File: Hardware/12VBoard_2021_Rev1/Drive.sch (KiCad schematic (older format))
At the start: 33 parts

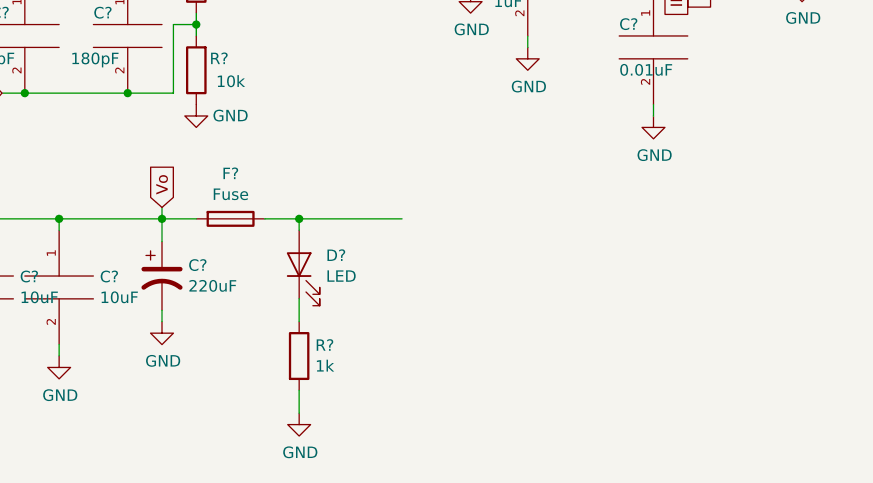
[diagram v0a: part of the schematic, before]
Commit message: current sense
started current sense circuit on hig current. added fuse and LED signal. started tiva wiring.
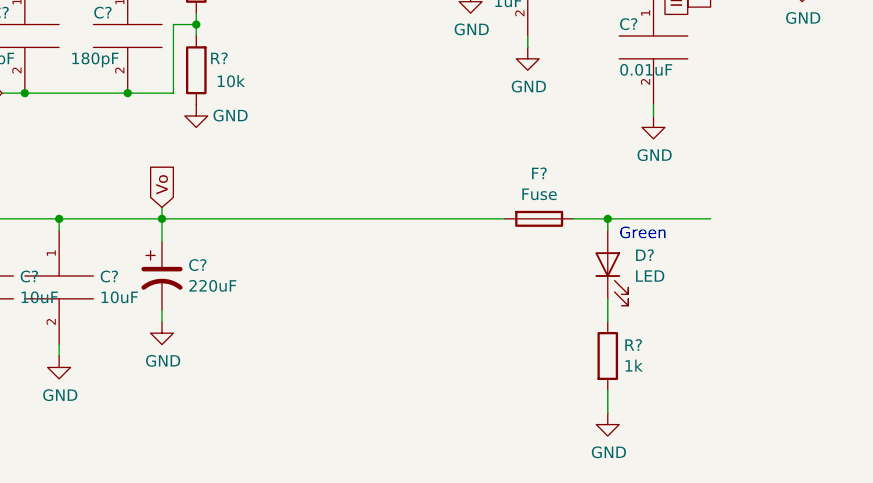
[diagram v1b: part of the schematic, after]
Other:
- note added: "Green"
- moved on the sheet: D?, F?, R?
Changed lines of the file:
@@
 L Device:Fuse F?
 U 1 1 5F97A572
-P 3150 3350
-F 0 "F?" V 2953 3350 50  0000 C CNN
-F 1 "Fuse" V 3044 3350 50  0000 C CNN
-F 2 "" V 3080 3350 50  0001 C CNN
-F 3 "~" H 3150 3350 50  0001 C CNN
-	1    3150 3350
+P 4500 3350
+F 0 "F?" V 4303 3350 50  0000 C CNN
+F 1 "Fuse" V 4394 3350 50  0000 C CNN
+F 2 "" V 4430 3350 50  0001 C CNN
+F 3 "~" H 4500 3350 50  0001 C CNN
+	1    4500 3350
 	0    1    1    0
 $EndComp
 Wire Wire Line
-	3000 3350 2850 3350
-Wire Wire Line
-	3300 3350 3450 3350
+	4650 3350 4800 3350
 $Comp
 L Device:R R?
 U 1 1 5F985FB9
-P 3450 3950
-F 0 "R?" H 3520 3996 50  0000 L CNN
-F 1 "1k" H 3520 3905 50  0000 L CNN
-F 2 "" V 3380 3950 50  0001 C CNN
-F 3 "~" H 3450 3950 50  0001 C CNN
-	1    3450 3950
+P 4800 3950
+F 0 "R?" H 4870 3996 50  0000 L CNN
+F 1 "1k" H 4870 3905 50  0000 L CNN
+F 2 "" V 4730 3950 50  0001 C CNN
+F 3 "~" H 4800 3950 50  0001 C CNN
+	1    4800 3950
 	1    0    0    -1
 $EndComp
@@
 L power:GND #PWR?
 U 1 1 5F98656C
-P 3450 4200
-F 0 "#PWR?" H 3450 3950 50  0001 C CNN
-F 1 "GND" H 3455 4027 50  0000 C CNN
-F 2 "" H 3450 4200 50  0001 C CNN
-F 3 "" H 3450 4200 50  0001 C CNN
-	1    3450 4200
+P 4800 4200
+F 0 "#PWR?" H 4800 3950 50  0001 C CNN
+F 1 "GND" H 4805 4027 50  0000 C CNN
+F 2 "" H 4800 4200 50  0001 C CNN
+F 3 "" H 4800 4200 50  0001 C CNN
+	1    4800 4200
 	1    0    0    -1
 $EndComp
@@
 L Device:LED D?
 U 1 1 5F986D88
-P 3450 3550
-F 0 "D?" V 3489 3433 50  0000 R CNN
-F 1 "LED" V 3398 3433 50  0000 R CNN
-F 2 "" H 3450 3550 50  0001 C CNN
-F 3 "~" H 3450 3550 50  0001 C CNN
-	1    3450 3550
+P 4800 3550
+F 0 "D?" V 4839 3433 50  0000 R CNN
+F 1 "LED" V 4748 3433 50  0000 R CNN
+F 2 "" H 4800 3550 50  0001 C CNN
+F 3 "~" H 4800 3550 50  0001 C CNN
+	1    4800 3550
 	0    -1   -1   0
 $EndComp
@@
 	2850 3800 2850 3750
 Wire Wire Line
-	3450 4200 3450 4100
+	4800 4200 4800 4100
 Wire Wire Line
-	3450 3800 3450 3700
+	4800 3800 4800 3700
 Wire Wire Line
-	3450 3400 3450 3350
+	4800 3400 4800 3350
 Wire Wire Line
-	3450 3350 3900 3350
-Connection ~ 3450 3350
+	4800 3350 5250 3350
+Connection ~ 4800 3350
 Wire Wire Line
 	3000 1950 2700 1950
+Text Notes 4850 3450 0    50   ~ 0
+Green
+Wire Wire Line
+	2850 3350 4350 3350
 $EndSCHEMATC

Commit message: current sense
finished adding current sensing to high current side, also started thinking about tiva pin connector layout
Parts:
- added R?: 5m, symbol Device:R
- added U?: INA198, Package_TO_SOT_SMD:SOT-23-5, symbol Amplifier_Current:INA198
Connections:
- net GND: now also U?.2 (GND)
- net Vo: now also R?.2, U?.4 (+); no longer F?.2
- new net: F?.2, R?.1, U?.5 (-)
- new net 5V: U?.3 (V+)
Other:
- moved on the sheet: D?, F?, R?
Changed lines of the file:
@@
 L Device:Fuse F?
 U 1 1 5F97A572
-P 4500 3350
-F 0 "F?" V 4303 3350 50  0000 C CNN
-F 1 "Fuse" V 4394 3350 50  0000 C CNN
-F 2 "" V 4430 3350 50  0001 C CNN
-F 3 "~" H 4500 3350 50  0001 C CNN
-	1    4500 3350
+P 4000 3350
+F 0 "F?" V 3803 3350 50  0000 C CNN
+F 1 "Fuse" V 3894 3350 50  0000 C CNN
+F 2 "" V 3930 3350 50  0001 C CNN
+F 3 "~" H 4000 3350 50  0001 C CNN
+	1    4000 3350
 	0    1    1    0
 $EndComp
 Wire Wire Line
-	4650 3350 4800 3350
+	4150 3350 4300 3350
 $Comp
 L Device:R R?
 U 1 1 5F985FB9
-P 4800 3950
-F 0 "R?" H 4870 3996 50  0000 L CNN
-F 1 "1k" H 4870 3905 50  0000 L CNN
-F 2 "" V 4730 3950 50  0001 C CNN
-F 3 "~" H 4800 3950 50  0001 C CNN
-	1    4800 3950
+P 4300 3950
+F 0 "R?" H 4370 3996 50  0000 L CNN
+F 1 "1k" H 4370 3905 50  0000 L CNN
+F 2 "" V 4230 3950 50  0001 C CNN
+F 3 "~" H 4300 3950 50  0001 C CNN
+	1    4300 3950
 	1    0    0    -1
 $EndComp
@@
 L power:GND #PWR?
 U 1 1 5F98656C
-P 4800 4200
-F 0 "#PWR?" H 4800 3950 50  0001 C CNN
-F 1 "GND" H 4805 4027 50  0000 C CNN
-F 2 "" H 4800 4200 50  0001 C CNN
-F 3 "" H 4800 4200 50  0001 C CNN
-	1    4800 4200
+P 4300 4200
+F 0 "#PWR?" H 4300 3950 50  0001 C CNN
+F 1 "GND" H 4305 4027 50  0000 C CNN
+F 2 "" H 4300 4200 50  0001 C CNN
+F 3 "" H 4300 4200 50  0001 C CNN
+	1    4300 4200
 	1    0    0    -1
 $EndComp
@@
 L Device:LED D?
 U 1 1 5F986D88
-P 4800 3550
-F 0 "D?" V 4839 3433 50  0000 R CNN
-F 1 "LED" V 4748 3433 50  0000 R CNN
-F 2 "" H 4800 3550 50  0001 C CNN
-F 3 "~" H 4800 3550 50  0001 C CNN
-	1    4800 3550
+P 4300 3550
+F 0 "D?" V 4339 3433 50  0000 R CNN
+F 1 "LED" V 4248 3433 50  0000 R CNN
+F 2 "" H 4300 3550 50  0001 C CNN
+F 3 "~" H 4300 3550 50  0001 C CNN
+	1    4300 3550
 	0    -1   -1   0
 $EndComp
@@
 	2850 3800 2850 3750
 Wire Wire Line
-	4800 4200 4800 4100
+	4300 4200 4300 4100
 Wire Wire Line
-	4800 3800 4800 3700
+	4300 3800 4300 3700
 Wire Wire Line
-	4800 3400 4800 3350
+	4300 3400 4300 3350
 Wire Wire Line
-	4800 3350 5250 3350
-Connection ~ 4800 3350
+	4300 3350 4750 3350
+Connection ~ 4300 3350
 Wire Wire Line
 	3000 1950 2700 1950
-Text Notes 4850 3450 0    50   ~ 0
+Text Notes 4350 3450 0    50   ~ 0
 Green
+$Comp
+L Amplifier_Current:INA198 U?
+U 1 1 5F8D1A0D
+P 3600 4100
+AR Path="/5F74F36B/5F8236F9/5F8D1A0D" Ref="U?"  Part="1"
+AR Path="/5F74F36B/5F821EB2/5F8D1A0D" Ref="U?"  Part="1"
+F 0 "U?" V 3650 3950 50  0000 R CNN
+F 1 "INA198" V 3750 4050 50  0000 R CNN
+F 2 "Package_TO_SOT_SMD:SOT-23-5" H 3600 4100 50  0001 C CNN
+F 3 "http://www.ti.com/lit/ds/symlink/ina193.pdf" H 3600 4100 50  0001 C CNN
+	1    3600 4100
+	0    -1   1    0
+$EndComp
+$Comp
+L Device:R R?
+U 1 1 5F8D1A13
+P 3600 3350
+AR Path="/5F74F36B/5F8236F9/5F8D1A13" Ref="R?"  Part="1"
+AR Path="/5F74F36B/5F821EB2/5F8D1A13" Ref="R?"  Part="1"
+F 0 "R?" V 3393 3350 50  0000 C CNN
+F 1 "5m" V 3484 3350 50  0000 C CNN
+F 2 "" V 3530 3350 50  0001 C CNN
+F 3 "~" H 3600 3350 50  0001 C CNN
+	1    3600 3350
+	0    1    1    0
+$EndComp
 Wire Wire Line
-	2850 3350 4350 3350
+	2850 3350 3450 3350
+Wire Wire Line
+	3500 3800 3500 3450
+Wire Wire Line
+	3500 3450 3450 3450
+Wire Wire Line
+	3450 3450 3450 3350
+Connection ~ 3450 3350
+Wire Wire Line
+	3700 3800 3700 3450
+Wire Wire Line
+	3700 3450 3750 3450
+Wire Wire Line
+	3750 3450 3750 3350
+$Comp
+L power:GND #PWR?
+U 1 1 5F8D1A21
+P 4100 4050
+AR Path="/5F74F36B/5F8236F9/5F8D1A21" Ref="#PWR?"  Part="1"
+AR Path="/5F74F36B/5F821EB2/5F8D1A21" Ref="#PWR?"  Part="1"
+F 0 "#PWR?" H 4100 3800 50  0001 C CNN
+F 1 "GND" H 4105 3877 50  0000 C CNN
+F 2 "" H 4100 4050 50  0001 C CNN
+F 3 "" H 4100 4050 50  0001 C CNN
+	1    4100 4050
+	1    0    0    -1
+$EndComp
+Wire Wire Line
+	4100 4050 4100 4000
+Wire Wire Line
+	4100 4000 3900 4000
+Text GLabel 3250 4000 0    50   Input ~ 0
+5V
+Wire Wire Line
+	3300 4000 3250 4000
+Wire Wire Line
+	3850 3350 3750 3350
+Connection ~ 3750 3350
 $EndSCHEMATC

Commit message: High current
Fisnished adding labes/tags
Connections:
- net DriveSense: now reaches U?.1
- net 12V15ADrive: now reaches D?.2 (A), F?.1
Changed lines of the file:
@@
 Wire Wire Line
 	4100 4000 3900 4000
-Text GLabel 3250 4000 0    50   Input ~ 0
-5V
 Wire Wire Line
 	3300 4000 3250 4000
@@
 	3850 3350 3750 3350
 Connection ~ 3750 3350
+Text HLabel 3250 4000 0    50   Output ~ 0
+5V
+Text HLabel 4750 3350 2    49   Output ~ 0
+12V15ADrive
+Text HLabel 3550 4500 0    49   Output ~ 0
+DriveSense
+Wire Wire Line
+	3600 4400 3600 4500
+Wire Wire Line
+	3600 4500 3550 4500
 $EndSCHEMATC

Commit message: Added Testpoints
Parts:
- added TP?: TestPoint, symbol Connector:TestPoint
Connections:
- net DriveSense: now also TP?.1
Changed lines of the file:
@@
 Wire Wire Line
 	3600 4500 3550 4500
+$Comp
+L Connector:TestPoint TP?
+U 1 1 5F8F4FF6
+P 3650 4500
+F 0 "TP?" V 3800 4600 50  0000 L CNN
+F 1 "TestPoint" V 3708 4527 50  0000 L CNN
+F 2 "" H 3850 4500 50  0001 C CNN
+F 3 "~" H 3850 4500 50  0001 C CNN
+	1    3650 4500
+	0    1    1    0
+$EndComp
+Wire Wire Line
+	3650 4500 3600 4500
+Connection ~ 3600 4500
 $EndSCHEMATC
